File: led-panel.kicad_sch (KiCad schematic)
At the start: 12 parts

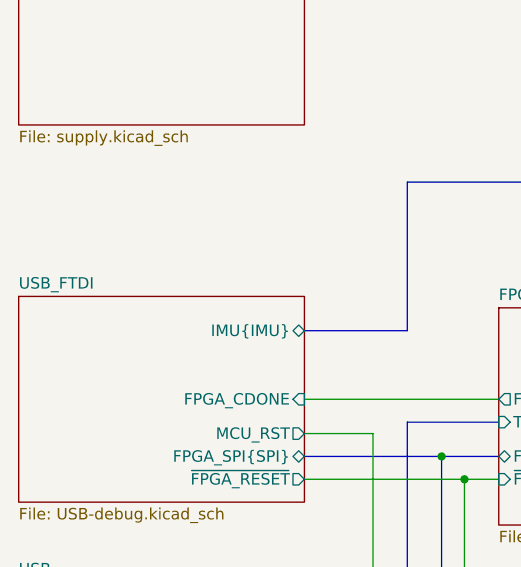
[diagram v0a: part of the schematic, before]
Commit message: made some stupid wrong changes to test the diff tool I'm building.
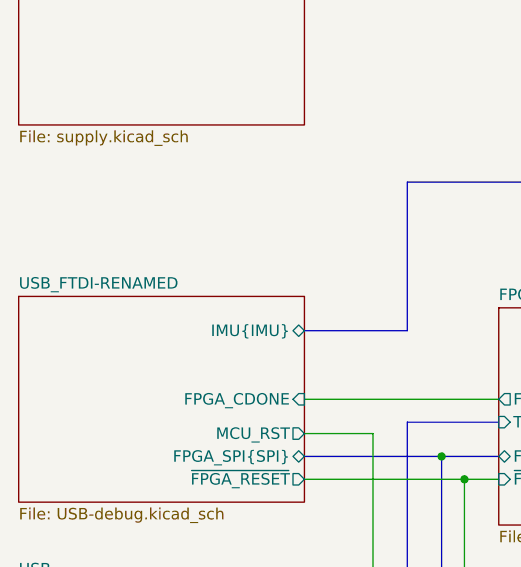
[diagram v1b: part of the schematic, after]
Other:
- sheet USB_FTDI renamed USB_FTDI-RENAMED
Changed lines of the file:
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@@
 		)
 		(instances
-			(project ""
+			(project "led-panel"
 				(path "/a86e1cab-ea0a-45e6-9194-d44b0d5c9450"
 					(reference "#PWR0201")
@@
 		)
 		(instances
-			(project ""
+			(project "led-panel"
 				(path "/a86e1cab-ea0a-45e6-9194-d44b0d5c9450"
 					(reference "H1")
@@
 		)
 		(instances
-			(project ""
+			(project "led-panel"
 				(path "/a86e1cab-ea0a-45e6-9194-d44b0d5c9450"
 					(reference "MP1")
@@
 			(color 0 0 0 0.0000)
 		)
-		(property "Sheetname" "USB_FTDI"
+		(property "Sheetname" "USB_FTDI-RENAMED"
 			(at 38.1 64.0584 0)
 			(effects
